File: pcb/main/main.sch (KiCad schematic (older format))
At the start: 6 parts, among them J1 USB_C_Receptacle_USB2.0, U1 LP3990MF-3.3_NOPB

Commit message: Added ESD protection to USB
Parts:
- added C3: 4.5n, symbol Device:C
- added D1: SP0502BAHT, Package_TO_SOT_SMD:SOT-23, symbol Power_Protection:SP0502BAHT
- added D2: SMAJ5.0A, Diode_SMD:D_SMA_Handsoldering, symbol Diode:SM6T22A
- added R3: 1M, symbol Device:R
- added U2: ATSAMD21G18A-AF, TQFP48_7x7MC_MCH, symbol ATSAMD:ATSAMD21G18A-AF
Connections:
- wire segments 30 -> 48
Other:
- moved on the sheet: R1, R2
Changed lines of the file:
@@
 Wire Wire Line
 	1550 4350 1550 4450
-Wire Wire Line
-	1550 4150 1550 4250
 $Comp
 L Device:R R1
 U 1 1 618AB323
-P 1950 3850
-F 0 "R1" V 1850 4000 50  0000 C CNN
-F 1 "5.1k" V 1850 3850 50  0000 C CNN
-F 2 "" V 1880 3850 50  0001 C CNN
-F 3 "~" H 1950 3850 50  0001 C CNN
-	1    1950 3850
+P 2350 3850
+F 0 "R1" V 2250 4000 50  0000 C CNN
+F 1 "5.1k" V 2250 3850 50  0000 C CNN
+F 2 "" V 2280 3850 50  0001 C CNN
+F 3 "~" H 2350 3850 50  0001 C CNN
+	1    2350 3850
 	0    1    1    0
 $EndComp
@@
 L Device:R R2
 U 1 1 618AC3FE
-P 1950 4000
-F 0 "R2" V 2050 4150 50  0000 C CNN
-F 1 "5.1k" V 2050 4000 50  0000 C CNN
-F 2 "" V 1880 4000 50  0001 C CNN
-F 3 "~" H 1950 4000 50  0001 C CNN
-	1    1950 4000
+P 2350 4000
+F 0 "R2" V 2450 4150 50  0000 C CNN
+F 1 "5.1k" V 2450 4000 50  0000 C CNN
+F 2 "" V 2280 4000 50  0001 C CNN
+F 3 "~" H 2350 4000 50  0001 C CNN
+	1    2350 4000
 	0    1    1    0
 $EndComp
@@
 $EndComp
 Wire Wire Line
-	1550 3850 1800 3850
-Wire Wire Line
-	1550 3950 1800 3950
-Wire Wire Line
-	1800 3950 1800 4000
+	2200 3950 2200 4000
 $Comp
 L power:GND #PWR0101
@@
 L power:GND #PWR0102
 U 1 1 618B17AD
-P 2250 3900
-F 0 "#PWR0102" H 2250 3650 50  0001 C CNN
-F 1 "GND" V 2255 3772 50  0000 R CNN
-F 2 "" H 2250 3900 50  0001 C CNN
-F 3 "" H 2250 3900 50  0001 C CNN
-	1    2250 3900
-	0    -1   -1   0
-$EndComp
-Wire Wire Line
-	2100 3850 2250 3850
-Wire Wire Line
-	2250 3850 2250 3900
-Wire Wire Line
-	2100 4000 2250 4000
-Wire Wire Line
-	2250 4000 2250 3900
-Connection ~ 2250 3900
+P 2650 4000
+F 0 "#PWR0102" H 2650 3750 50  0001 C CNN
+F 1 "GND" V 2655 3872 50  0000 R CNN
+F 2 "" H 2650 4000 50  0001 C CNN
+F 3 "" H 2650 4000 50  0001 C CNN
+	1    2650 4000
+	0    -1   -1   0
+$EndComp
+Wire Wire Line
+	2500 3850 2650 3850
+Wire Wire Line
+	2500 4000 2650 4000
 $Comp
 L power:GND #PWR0103
@@
 Wire Wire Line
 	1550 3650 1650 3650
-Wire Wire Line
-	1650 3650 1650 3400
 $Comp
 L power:PWR_FLAG #FLG0102
 U 1 1 618FAD3C
-P 1650 3400
-F 0 "#FLG0102" H 1650 3475 50  0001 C CNN
-F 1 "PWR_FLAG" V 1650 3528 50  0000 L CNN
-F 2 "" H 1650 3400 50  0001 C CNN
-F 3 "~" H 1650 3400 50  0001 C CNN
-	1    1650 3400
-	0    1    1    0
-$EndComp
-Connection ~ 1650 3400
-Wire Wire Line
-	1650 3400 1650 3250
+P 1650 3300
+F 0 "#FLG0102" H 1650 3375 50  0001 C CNN
+F 1 "PWR_FLAG" V 1650 3428 50  0000 L CNN
+F 2 "" H 1650 3300 50  0001 C CNN
+F 3 "~" H 1650 3300 50  0001 C CNN
+	1    1650 3300
+	0    1    1    0
+$EndComp
 NoConn ~ 1550 4750
 NoConn ~ 1550 4850
@@
 Wire Wire Line
 	950  5250 950  5300
-Wire Wire Line
-	650  5250 650  5150
-Wire Wire Line
-	650  5250 950  5250
-Wire Wire Line
-	1550 4250 2550 4250
-Connection ~ 1550 4250
-Wire Wire Line
-	1550 4350 2550 4350
-Connection ~ 1550 4350
+$Comp
+L ATSAMD:ATSAMD21G18A-AF U2
+U 1 1 618D4AB8
+P 5700 2150
+F 0 "U2" H 6700 2537 60  0000 C CNN
+F 1 "ATSAMD21G18A-AF" H 6700 2431 60  0000 C CNN
+F 2 "TQFP48_7x7MC_MCH" H 6700 2390 60  0001 C CNN
+F 3 "" H 5700 2150 60  0000 C CNN
+	1    5700 2150
+	1    0    0    -1
+$EndComp
+$Comp
+L Device:C C3
+U 1 1 618DADD9
+P 650 6200
+F 0 "C3" H 535 6154 50  0000 R CNN
+F 1 "4.5n" H 535 6245 50  0000 R CNN
+F 2 "" H 688 6050 50  0001 C CNN
+F 3 "~" H 650 6200 50  0001 C CNN
+	1    650  6200
+	-1   0    0    1
+$EndComp
+$Comp
+L Device:R R3
+U 1 1 618DB9D4
+P 1050 6200
+F 0 "R3" H 1120 6246 50  0000 L CNN
+F 1 "1M" H 1120 6155 50  0000 L CNN
+F 2 "" V 980 6200 50  0001 C CNN
+F 3 "~" H 1050 6200 50  0001 C CNN
+	1    1050 6200
+	1    0    0    -1
+$EndComp
+Wire Wire Line
+	650  5150 650  6050
+Wire Wire Line
+	650  6050 1050 6050
+Connection ~ 650  6050
+Wire Wire Line
+	650  6350 1050 6350
+$Comp
+L power:GND #PWR01
+U 1 1 618E2E72
+P 1050 6050
+F 0 "#PWR01" H 1050 5800 50  0001 C CNN
+F 1 "GND" H 1055 5877 50  0000 C CNN
+F 2 "" H 1050 6050 50  0001 C CNN
+F 3 "" H 1050 6050 50  0001 C CNN
+	1    1050 6050
+	-1   0    0    1
+$EndComp
+Connection ~ 1050 6050
+$Comp
+L Power_Protection:SP0502BAHT D1
+U 1 1 618FEEA4
+P 2200 4750
+F 0 "D1" V 2542 4750 50  0000 C CNN
+F 1 "SP0502BAHT" V 2451 4750 50  0000 C CNN
+F 2 "Package_TO_SOT_SMD:SOT-23" H 2425 4700 50  0001 L CNN
+F 3 "http://www.littelfuse.com/~/media/files/littelfuse/technical%20resources/documents/data%20sheets/sp05xxba.pdf" H 2325 4875 50  0001 C CNN
+	1    2200 4750
+	0    -1   -1   0
+$EndComp
+$Comp
+L power:GND #PWR02
+U 1 1 61902C7A
+P 2500 4750
+F 0 "#PWR02" H 2500 4500 50  0001 C CNN
+F 1 "GND" V 2505 4622 50  0000 R CNN
+F 2 "" H 2500 4750 50  0001 C CNN
+F 3 "" H 2500 4750 50  0001 C CNN
+	1    2500 4750
+	0    -1   -1   0
+$EndComp
+Wire Wire Line
+	2400 4750 2500 4750
+Wire Wire Line
+	1550 4150 1550 4250
+Wire Wire Line
+	1800 4650 2000 4650
+Wire Wire Line
+	1350 4600 1350 4450
+Wire Wire Line
+	1350 4450 1550 4450
+Connection ~ 1550 4450
+Wire Wire Line
+	1550 4450 1650 4450
+Wire Wire Line
+	1650 4450 1650 4850
+Wire Wire Line
+	1650 4850 2000 4850
+Wire Wire Line
+	1800 4300 2950 4300
+Wire Wire Line
+	2950 4300 2950 4650
+Wire Wire Line
+	2950 4650 3250 4650
+Wire Wire Line
+	1800 4300 1800 4650
+Wire Wire Line
+	1650 4850 1650 5050
+Wire Wire Line
+	1650 5050 2950 5050
+Wire Wire Line
+	2950 5050 2950 4850
+Wire Wire Line
+	2950 4850 3250 4850
+Connection ~ 1650 4850
+$Comp
+L Diode:SM6T22A D2
+U 1 1 61925272
+P 2350 3650
+F 0 "D2" H 2350 3867 50  0000 C CNN
+F 1 "SMAJ5.0A" H 2350 3776 50  0000 C CNN
+F 2 "Diode_SMD:D_SMA_Handsoldering" H 2350 3450 50  0001 C CNN
+F 3 "https://www.st.com/resource/en/datasheet/sm6t.pdf" H 2300 3650 50  0001 C CNN
+	1    2350 3650
+	1    0    0    -1
+$EndComp
+Wire Wire Line
+	2650 3650 2650 3850
+Connection ~ 2650 3850
+Connection ~ 1650 3300
+Wire Wire Line
+	1650 3300 1650 3250
+Wire Wire Line
+	1650 3300 1650 3650
+Wire Wire Line
+	2500 3650 2650 3650
+Connection ~ 2650 4000
+Wire Wire Line
+	2650 3850 2650 4000
+Wire Wire Line
+	1550 4150 1800 4150
+Wire Wire Line
+	1800 4150 1800 4300
+Connection ~ 1550 4150
+Connection ~ 1800 4300
+Wire Wire Line
+	2200 3650 1650 3650
+Connection ~ 1650 3650
+Wire Wire Line
+	1550 3850 2200 3850
+Wire Wire Line
+	2200 3950 1550 3950
 $EndSCHEMATC

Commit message: Complete circuit + footprint association
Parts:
- removed D1: SP0502BAHT, Package_TO_SOT_SMD:SOT-23, symbol Power_Protection:SP0502BAHT
- removed D2: SMAJ5.0A, Diode_SMD:D_SMA_Handsoldering, symbol Diode:SM6T22A
- removed J1: USB_C_Receptacle_USB2.0, symbol Connector:USB_C_Receptacle_USB2.0
- removed R3: 1M, symbol Device:R
- removed U1: LP3990MF-3.3_NOPB, DBV0005A_N, symbol LP3990MF-3.3/NOPB:LP3990MF-3.3_NOPB
- removed U2: ATSAMD21G18A-AF, TQFP48_7x7MC_MCH, symbol ATSAMD:ATSAMD21G18A-AF
- added C4: 100n, Capacitor_SMD:C_0603_1608Metric_Pad1.08x0.95mm_HandSolder, symbol Device:C
- added J1, J3: Conn_01x08, Connector_PinHeader_2.54mm:PinHeader_1x08_P2.54mm_Vertical, symbol Connector_Generic:Conn_01x08
- added J2: Conn_ARM_JTAG_SWD_10, Connector_PinHeader_1.27mm:PinHeader_2x05_P1.27mm_Vertical_SMD, symbol Connector:Conn_ARM_JTAG_SWD_10
- added SW1: SW_Push, Button_Switch_SMD:SW_Push_1P1T_NO_6x6mm_H9.5mm, symbol Switch:SW_Push
- added U1: ATSAMD21E18A-AF, ATSAMD:ATSAMD21E18A-AF, symbol ATSAMD:ATSAMD21E18A-AF
- C1, C2: value 1u -> 100n; footprint Capacitor_SMD:C_0805_2012Metric_Pad1.18x1.45mm_HandSolder -> Capacitor_SMD:C_0603_1608Metric_Pad1.08x0.95mm_HandSolder
- C3: value 4.5n -> 1u; footprint (none) -> Capacitor_SMD:C_0805_2012Metric_Pad1.18x1.45mm_HandSolder
- R1: value 5.1k -> 330; footprint (none) -> Resistor_SMD:R_0603_1608Metric_Pad0.98x0.95mm_HandSolder
- R2: value 5.1k -> 2.2k; footprint (none) -> Resistor_SMD:R_0603_1608Metric_Pad0.98x0.95mm_HandSolder
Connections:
- net labels added: +3.3V, +3.3VA
- net labels removed: +3V3, +5V
- wire segments 48 -> 96
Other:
- note added: "Analog pin breakout\n"
- note added: "Digital pin breakout\n"

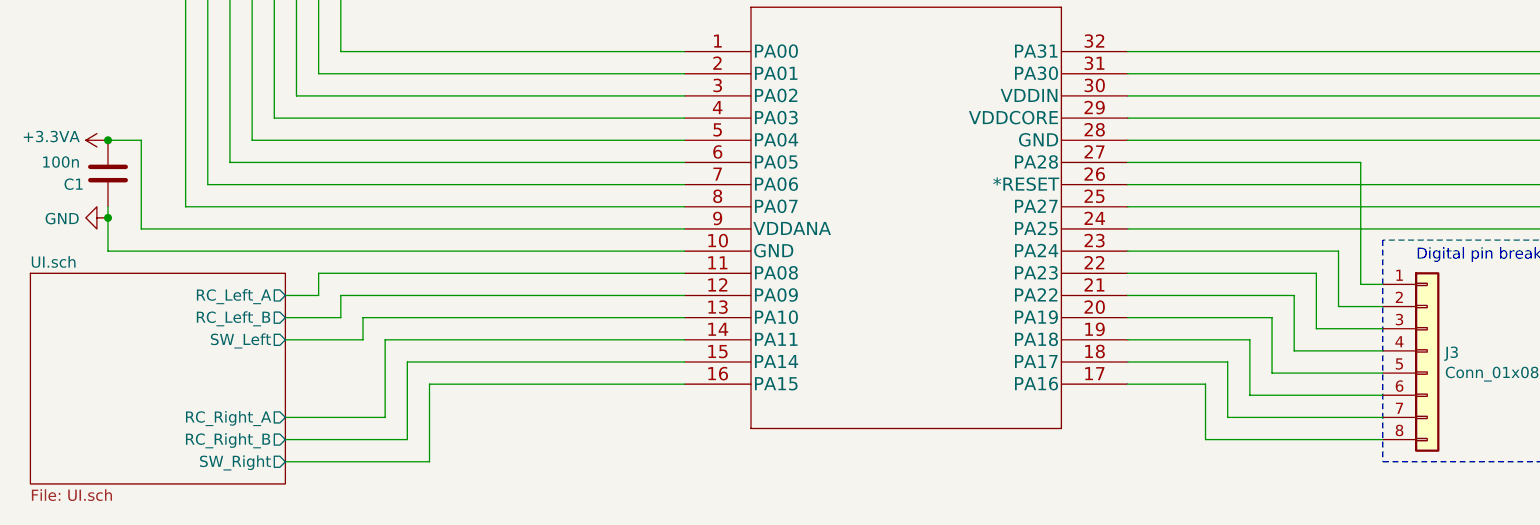
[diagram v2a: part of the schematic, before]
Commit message: Finished PCB layout
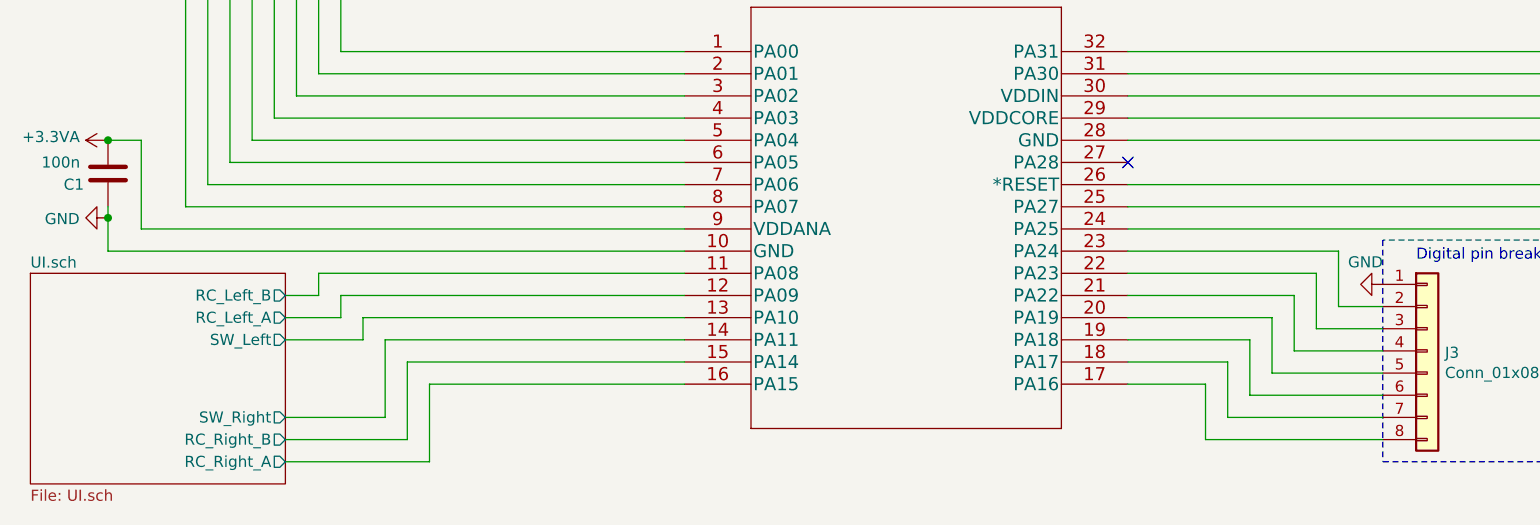
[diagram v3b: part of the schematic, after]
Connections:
- net GND: now also J3.1 (Pin_1)
- net UI.sch/RC_Left_A: now also U1.12 (PA09); no longer U1.11 (PA08)
- net UI.sch/RC_Left_B: now also U1.11 (PA08); no longer U1.12 (PA09)
- net UI.sch/RC_Right_A: now also U1.16 (PA15); no longer U1.14 (PA11)
- net UI.sch/SW_Right: now also U1.14 (PA11); no longer U1.16 (PA15)
- net at U1.27 (PA28): no longer J3.1 (Pin_1)
- no-connect marks 3 -> 4
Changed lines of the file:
@@
 F0 "UI.sch" 50
 F1 "UI.sch" 50
-F2 "RC_Left_A" O R 1850 4400 50
-F3 "RC_Left_B" O R 1850 4500 50
+F2 "RC_Left_A" O R 1850 4500 50
+F3 "RC_Left_B" O R 1850 4400 50
 F4 "SW_Left" O R 1850 4600 50
-F5 "RC_Right_A" O R 1850 4950 50
+F5 "RC_Right_A" O R 1850 5150 50
 F6 "RC_Right_B" O R 1850 5050 50
-F7 "SW_Right" O R 1850 5150 50
+F7 "SW_Right" O R 1850 4950 50
 $EndSheet
 Wire Wire Line
@@
 Wire Wire Line
 	8550 3600 8800 3600
-Wire Wire Line
-	6800 4350 6700 4350
-Wire Wire Line
-	6700 4350 6700 3800
-Wire Wire Line
-	6700 3800 5650 3800
 Text Notes 6950 4250 0    50   ~ 0
 Digital pin breakout\n
@@
 	0    -1   -1   0
 $EndComp
+NoConn ~ 5650 3800
+$Comp
+L power:GND #PWR?
+U 1 1 619E6C31
+P 6800 4350
+F 0 "#PWR?" H 6800 4100 50  0001 C CNN
+F 1 "GND" V 6700 4350 50  0000 R CNN
+F 2 "" H 6800 4350 50  0001 C CNN
+F 3 "" H 6800 4350 50  0001 C CNN
+	1    6800 4350
+	0    1    1    0
+$EndComp
 $EndSCHEMATC
